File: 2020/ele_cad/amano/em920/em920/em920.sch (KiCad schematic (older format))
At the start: 4 parts, among them J1 Conn_01x06, U1 ATtiny85-20PU, U2 TY92SS

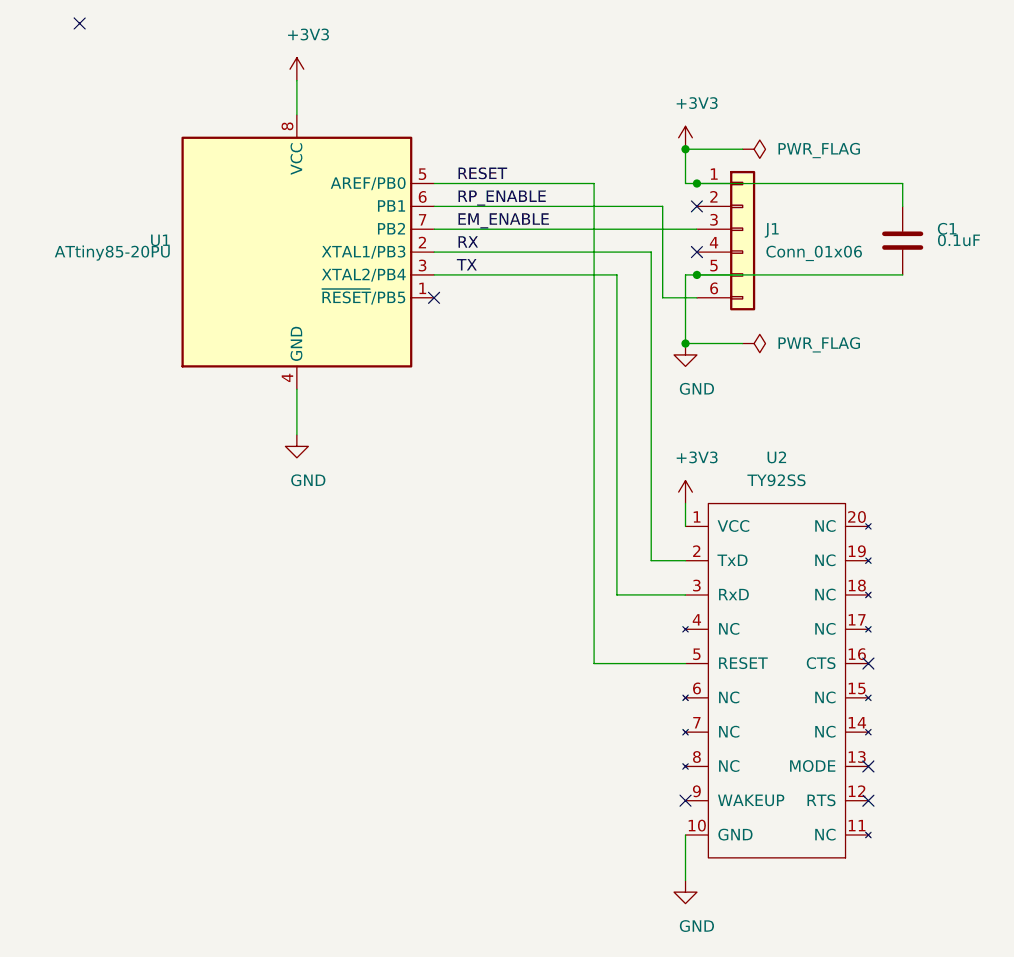
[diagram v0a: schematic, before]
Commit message: em920のフォルダ構造を変更
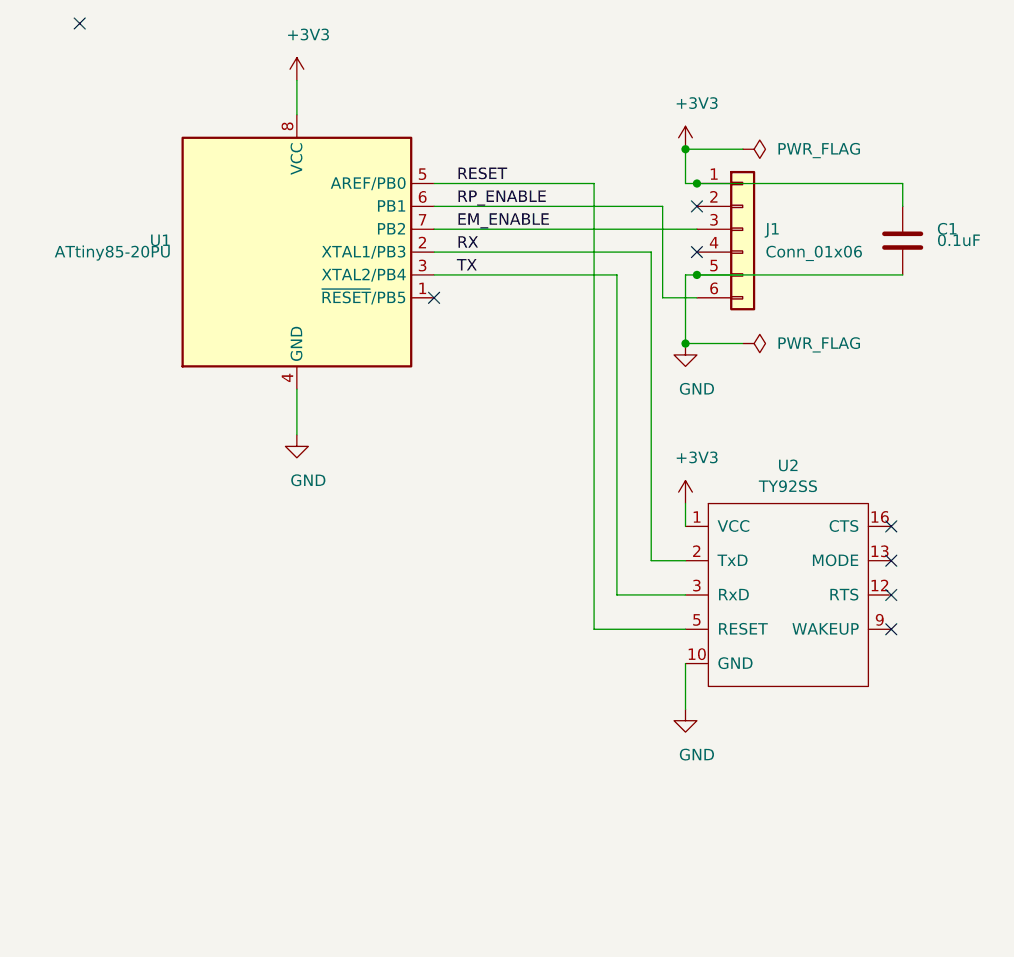
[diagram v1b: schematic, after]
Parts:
- removed U2: TY92SS, em920_lib:TY92SS, symbol em920-rescue:TY92SS-em920
- added U2: TY92SS, em920_lib:TY92SS, symbol em920_lib:TY92SS
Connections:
- net +3V3: now also U2.1 (VCC)
- net GND: now also U2.10 (GND)
- net RESET: now also U2.5 (RESET)
- net RX: now also U2.2 (TxD)
- net TX: now also U2.3 (RxD)
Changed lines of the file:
@@
 L power:GND #PWR04
 U 1 1 60FD4012
-P 3500 4250
-F 0 "#PWR04" H 3500 4000 50  0001 C CNN
-F 1 "GND" H 3550 4050 50  0000 C CNN
-F 2 "" H 3500 4250 50  0001 C CNN
-F 3 "" H 3500 4250 50  0001 C CNN
-	1    3500 4250
+P 3500 3500
+F 0 "#PWR04" H 3500 3250 50  0001 C CNN
+F 1 "GND" H 3550 3300 50  0000 C CNN
+F 2 "" H 3500 3500 50  0001 C CNN
+F 3 "" H 3500 3500 50  0001 C CNN
+	1    3500 3500
 	1    0    0    -1
 $EndComp
 Wire Wire Line
-	3500 4050 3500 4250
+	3500 3300 3500 3500
 Wire Wire Line
 	2400 1600 3200 1600
@@
 	3500 1050 3750 1050
 Connection ~ 3500 1050
-NoConn ~ 4300 3300
-NoConn ~ 4300 3750
-NoConn ~ 4300 3900
-NoConn ~ 3500 3900
 NoConn ~ 850  500
 Wire Wire Line
@@
 $EndComp
 $Comp
-L em920-rescue:TY92SS-em920 U2
-U 1 1 60FCC105
-P 3500 2700
-F 0 "U2" H 3900 3000 50  0000 C CNN
-F 1 "TY92SS" H 3900 2900 50  0000 C CNN
-F 2 "em920_lib:TY92SS" H 3500 2700 50  0001 C CNN
-F 3 "" H 3500 2700 50  0001 C CNN
-F 4 "em920:TY92SS" H 3500 2700 50  0001 C CNN "Footprint"
-F 5 "TY92SS" H 3500 2700 50  0001 C CNN "Value"
-	1    3500 2700
-	1    0    0    -1
-$EndComp
-$Comp
 L Connector_Generic:Conn_01x06 J1
 U 1 1 60FC3A2C
@@
 $EndComp
 Wire Wire Line
-	3100 3300 3500 3300
+	3100 3150 3500 3150
 Text Label 2500 1200 0    50   ~ 0
 RESET
@@
 	2400 1200 3100 1200
 Wire Wire Line
-	3100 1200 3100 3300
+	3100 1200 3100 3150
 NoConn ~ 2400 1700
+$Comp
+L em920_lib:TY92SS U2
+U 1 1 6123A86E
+P 3500 2700
+F 0 "U2" H 3950 2965 50  0000 C CNN
+F 1 "TY92SS" H 3950 2874 50  0000 C CNN
+F 2 "em920_lib:TY92SS" H 3500 2700 50  0001 C CNN
+F 3 "" H 3500 2700 50  0001 C CNN
+	1    3500 2700
+	1    0    0    -1
+$EndComp
+NoConn ~ 4400 2700
+NoConn ~ 4400 2850
+NoConn ~ 4400 3000
+NoConn ~ 4400 3150
 $EndSCHEMATC
